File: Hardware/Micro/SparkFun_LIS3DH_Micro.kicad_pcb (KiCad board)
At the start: 2 copper layers, 19 x 7.6 mm, 34 parts, among them J1 PTH_1x1mm, J2 Qwiic_RA, J5 PTH_1x1mm, U1 LIS3DH

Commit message: Fixes silk on micro, and adds note about 22AWG wire with PTH
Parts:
- removed kibuzzard-6841DB16: G***, kibuzzard-6841DB16
- removed kibuzzard-6841DB2D: G***, kibuzzard-6841DB2D
- added kibuzzard-68489829: G***, kibuzzard-68489829, F.Cu at (126.1, 109.5)
- added kibuzzard-68489831: G***, kibuzzard-68489831, F.Cu at (126.2, 104.6)

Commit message: Updates LIS3DH in the micro board according to new changes
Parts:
- U1: footprint SparkFun-Sensor:LGA-16-3X3 -> SparkFun-Sensor:ST_LGA-16_3x3mm_P0.5mm_5x3
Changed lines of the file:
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@@
 		(property ki_fp_filters "Fiducial*")
 		(sheetname "/")
-		(sheetfile "SparkFun_LIS3DH_Mini.kicad_sch")
+		(sheetfile "SparkFun_LIS3DH_Micro.kicad_sch")
 		(attr smd)
 		(fp_circle
@@
 				(font
 					(size 0.001 0.001)
+					(thickness 0.15)
 				)
 			)
@@
 				(font
 					(size 0.001 0.001)
+					(thickness 0.15)
 				)
 			)
@@
 		(property ki_fp_filters "R_*")
 		(sheetname "/")
-		(sheetfile "SparkFun_LIS3DH_Mini.kicad_sch")
+		(sheetfile "SparkFun_LIS3DH_Micro.kicad_sch")
 		(attr smd)
 		(fp_line
@@
 		(property ki_fp_filters "Connector*:*_1x??_*")
 		(sheetname "/")
-		(sheetfile "SparkFun_LIS3DH_Mini.kicad_sch")
+		(sheetfile "SparkFun_LIS3DH_Micro.kicad_sch")
 		(fp_poly
 			(pts
@@
 		(property ki_fp_filters "Connector*:*_1x??_*")
 		(sheetname "/")
-		(sheetfile "SparkFun_LIS3DH_Mini.kicad_sch")
+		(sheetfile "SparkFun_LIS3DH_Micro.kicad_sch")
 		(fp_poly
 			(pts
@@
 		(property ki_fp_filters "R_*")
 		(sheetname "/")
-		(sheetfile "SparkFun_LIS3DH_Mini.kicad_sch")
+		(sheetfile "SparkFun_LIS3DH_Micro.kicad_sch")
 		(attr smd)
 		(fp_line
@@
 		(property ki_fp_filters "R_*")
 		(sheetname "/")
-		(sheetfile "SparkFun_LIS3DH_Mini.kicad_sch")
+		(sheetfile "SparkFun_LIS3DH_Micro.kicad_sch")
 		(attr smd)
 		(fp_line
@@
 		(property ki_fp_filters "LED* LED_SMD:* LED_THT:*")
 		(sheetname "/")
-		(sheetfile "SparkFun_LIS3DH_Mini.kicad_sch")
+		(sheetfile "SparkFun_LIS3DH_Micro.kicad_sch")
 		(attr smd)
 		(fp_line
@@
 		(property ki_fp_filters "Fiducial*")
 		(sheetname "/")
-		(sheetfile "SparkFun_LIS3DH_Mini.kicad_sch")
+		(sheetfile "SparkFun_LIS3DH_Micro.kicad_sch")
 		(attr smd)
 		(fp_circle
@@
 		(property ki_fp_filters "C_*")
 		(sheetname "/")
-		(sheetfile "SparkFun_LIS3DH_Mini.kicad_sch")
+		(sheetfile "SparkFun_LIS3DH_Micro.kicad_sch")
 		(attr smd)
 		(fp_line
@@
 		)
 	)
-	(footprint "SparkFun-Sensor:LGA-16-3X3"
+	(footprint "SparkFun-Sensor:ST_LGA-16_3x3mm_P0.5mm_5x3"
 		(layer "F.Cu")
 		(at 132.156 106.996 180)
-		(descr "16-Pin Land Grid Array (LGA) (3 x 3 mm)\n\nhttps://www.sparkfun.com/datasheets/Sensors/Accelerometer/LIS331HH.pdf Datasheet\n\nSpecifications:\n\n• Pin Count: 16\n• Area: 3.0 x 3.0 x 1.0 mm\n• Pitch: 0.5 mm\n\nDevices Using:\n\n• LIS331\n• LIS3DH")
+		(descr "ST 16-Pin Land Grid Array (LGA) (3 x 3 mm)")
+		(tags "SparkFun")
 		(property "Reference" "U1"
 			(at 0 -1.905 180)
 			(unlocked yes)
 			(layer "F.Fab")
-			(hide yes)
 			(effects
 				(font
@@
 			(unlocked yes)
 			(layer "F.Fab")
-			(hide yes)
 			(effects
 				(font
@@
 		)
 		(property "Datasheet" "https://www.st.com/en/mems-and-sensors/lis3dh.html"
-			(at 0 0 0)
+			(at 0 0 180)
 			(layer "F.Fab")
 			(hide yes)
@@
 		)
 		(property "Description" "The LIS3DH has dynamically user-selectable full scales of ±2g/±4g/±8g/±16g and is capable of measuring accelerations with output data rates from 1 Hz to 5.3 kHz."
-			(at 0 0 0)
+			(at 0 0 180)
 			(layer "F.Fab")
 			(hide yes)
@@
 		)
 		(sheetname "/")
-		(sheetfile "SparkFun_LIS3DH_Mini.kicad_sch")
+		(sheetfile "SparkFun_LIS3DH_Micro.kicad_sch")
 		(fp_line
 			(start 1.7 1.3722)
@@
 		)
 		(fp_circle
-			(center -2.2 -1.6)
-			(end -2.073 -1.6)
+			(center -2.2 -1.5)
+			(end -2.3 -1.5)
 			(stroke
-				(width 0.254)
+				(width 0.2)
 				(type solid)
 			)
@@
 		)
 		(fp_line
+			(start 0 1)
+			(end 0.2 0.8)
+			(stroke
+				(width 0.1)
+				(type default)
+			)
+			(layer "F.Fab")
+		)
+		(fp_line
+			(start 0 1)
+			(end -0.2 0.8)
+			(stroke
+				(width 0.1)
+				(type default)
+			)
+			(layer "F.Fab")
+		)
+		(fp_line
+			(start 0 0)
+			(end 0 1)
+			(stroke
+				(width 0.1)
+				(type default)
+			)
+			(layer "F.Fab")
+		)
+		(fp_line
+			(start 0 0)
+			(end -1 0)
+			(stroke
+				(width 0.1)
+				(type default)
+			)
+			(layer "F.Fab")
+		)
+		(fp_line
+			(start -1 0)
+			(end -0.8 0.2)
+			(stroke
+				(width 0.1)
+				(type default)
+			)
+			(layer "F.Fab")
+		)
+		(fp_line
+			(start -1 0)
+			(end -0.8 -0.2)
+			(stroke
+				(width 0.1)
+				(type default)
+			)
+			(layer "F.Fab")
+		)
+		(fp_line
 			(start -1.5 1.5)
 			(end -1.5 -1.5)
@@
 			(layer "F.Fab")
 		)
+		(fp_circle
+			(center 0 0)
+			(end -0.05 0)
+			(stroke
+				(width 0.1)
+				(type default)
+			)
+			(fill no)
+			(layer "F.Fab")
+		)
+		(fp_circle
+			(center 0 0)
+			(end -0.25 0)
+			(stroke
+				(width 0.1)
+				(type default)
+			)
+			(fill no)
+			(layer "F.Fab")
+		)
+		(fp_text user "Z"
+			(at 0.4 -0.35 180)
+			(unlocked yes)
+			(layer "F.Fab")
+			(effects
+				(font
+					(size 0.25 0.25)
+					(thickness 0.0625)
+				)
+			)
+		)
+		(fp_text user "X"
+			(at -0.8 -0.5 180)
+			(unlocked yes)
+			(layer "F.Fab")
+			(effects
+				(font
+					(size 0.25 0.25)
+					(thickness 0.0625)
+				)
+			)
+		)
+		(fp_text user "Y"
+			(at 0.25 0.5 180)
+			(unlocked yes)
+			(layer "F.Fab")
+			(effects
+				(font
+					(size 0.25 0.25)
+					(thickness 0.0625)
+				)
+			)
+		)
 		(pad "1" smd rect
 			(at -1.4 -1)
@@
 		)
 		(embedded_fonts no)
-		(model "${SPARKFUN_KICAD_LIBRARY}/Footprints/SparkFun-3D-models/Sensor/LIS3DH_LGA-16_3x3x1mm.step"
+		(model "${SPARKFUN_KICAD_LIBRARY}/Footprints/SparkFun-3D-models/Semiconductor-Standard/LGA-16_3x3x1mm.step"
 			(offset
 				(xyz 0 0 0)
@@
 		(property ki_fp_filters "Connector*:*_1x??_*")
 		(sheetname "/")
-		(sheetfile "SparkFun_LIS3DH_Mini.kicad_sch")
+		(sheetfile "SparkFun_LIS3DH_Micro.kicad_sch")
 		(attr smd)
 		(fp_line
@@
 		(property ki_fp_filters "R_*")
 		(sheetname "/")
-		(sheetfile "SparkFun_LIS3DH_Mini.kicad_sch")
+		(sheetfile "SparkFun_LIS3DH_Micro.kicad_sch")
 		(attr smd)
 		(fp_line
@@
 				(font
 					(size 0.001 0.001)
+					(thickness 0.15)
 				)
 			)
@@
 				(font
 					(size 0.001 0.001)
+					(thickness 0.15)
 				)
 			)
@@
 		)
 		(sheetname "/")
-		(sheetfile "SparkFun_LIS3DH_Mini.kicad_sch")
+		(sheetfile "SparkFun_LIS3DH_Micro.kicad_sch")
 		(attr exclude_from_pos_files exclude_from_bom)
 		(fp_text user " https://creativecommons.org/licenses/by-sa/4.0/"
@@
 		(property ki_fp_filters "C_*")
 		(sheetname "/")
-		(sheetfile "SparkFun_LIS3DH_Mini.kicad_sch")
+		(sheetfile "SparkFun_LIS3DH_Micro.kicad_sch")
 		(attr smd)
 		(fp_line
@@
 		(property ki_fp_filters "Fiducial*")
 		(sheetname "/")
-		(sheetfile "SparkFun_LIS3DH_Mini.kicad_sch")
+		(sheetfile "SparkFun_LIS3DH_Micro.kicad_sch")
 		(fp_circle
 			(center 0 0)
@@
 		(property ki_fp_filters "SolderJumper*Open*")
 		(sheetname "/")
-		(sheetfile "SparkFun_LIS3DH_Mini.kicad_sch")
+		(sheetfile "SparkFun_LIS3DH_Micro.kicad_sch")
 		(fp_line
 			(start 1.1176 -0.762)
@@
 		(property ki_fp_filters "SolderJumper*Bridged123*")
 		(sheetname "/")
-		(sheetfile "SparkFun_LIS3DH_Mini.kicad_sch")
+		(sheetfile "SparkFun_LIS3DH_Micro.kicad_sch")
 		(attr allow_soldermask_bridges)
 		(net_tie_pad_groups "1,2,3")
@@
 		(property ki_fp_filters "Pin* Test*")
 		(sheetname "/")
-		(sheetfile "SparkFun_LIS3DH_Mini.kicad_sch")
+		(sheetfile "SparkFun_LIS3DH_Micro.kicad_sch")
 		(fp_circle
 			(center 0 0)
@@
 		(property ki_fp_filters "Pin* Test*")
 		(sheetname "/")
-		(sheetfile "SparkFun_LIS3DH_Mini.kicad_sch")
+		(sheetfile "SparkFun_LIS3DH_Micro.kicad_sch")
 		(fp_circle
 			(center 0 0)
@@
 		(property ki_fp_filters "SolderJumper*Bridged*")
 		(sheetname "/")
-		(sheetfile "SparkFun_LIS3DH_Mini.kicad_sch")
+		(sheetfile "SparkFun_LIS3DH_Micro.kicad_sch")
 		(attr allow_soldermask_bridges)
 		(net_tie_pad_groups "1,2")
@@
 		(property ki_fp_filters "Fiducial*")
 		(sheetname "/")
-		(sheetfile "SparkFun_LIS3DH_Mini.kicad_sch")
+		(sheetfile "SparkFun_LIS3DH_Micro.kicad_sch")
 		(attr smd)
 		(fp_circle
@@
 		(property ki_fp_filters "Fiducial*")
 		(sheetname "/")
-		(sheetfile "SparkFun_LIS3DH_Mini.kicad_sch")
+		(sheetfile "SparkFun_LIS3DH_Micro.kicad_sch")
 		(attr smd)
 		(fp_circle
@@
 		(property ki_fp_filters "Pin* Test*")
 		(sheetname "/")
-		(sheetfile "SparkFun_LIS3DH_Mini.kicad_sch")
+		(sheetfile "SparkFun_LIS3DH_Micro.kicad_sch")
 		(fp_circle
 			(center 0 0)
@@
 		(property ki_fp_filters "Pin* Test*")
 		(sheetname "/")
-		(sheetfile "SparkFun_LIS3DH_Mini.kicad_sch")
+		(sheetfile "SparkFun_LIS3DH_Micro.kicad_sch")
 		(fp_circle
 			(center 0 0)

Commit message: Updates the 1 mm PTH part
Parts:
- D1: footprint SparkFun-LED:LED_0402_1005Metric -> SparkFun-LED:LED_0402_1005Metric_Red
- J1, J5: footprint SparkFun-Connector:1x01_PTH_1x1mm -> SparkFun-Connector:1x01_1x1mm
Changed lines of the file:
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@@
 		)
 	)
-	(footprint "SparkFun-Connector:1x01_PTH_1x1mm"
+	(footprint "SparkFun-Connector:1x01_1x1mm"
 		(layer "F.Cu")
 		(at 128.346 104.456 180)
 		(descr "Plated Through Hole - No Silk Outline\n\nSpecifications:\n\n• Pin count:1\n• Pin pitch:0.1mm\n• Hole Size: .7mm\n• Annular Ring: 1.2mm\n\nMade for the small  https://www.sparkfun.com/products/18221  1mm Pitch Headers.")
+		(tags "SparkFun")
 		(property "Reference" "J5"
 			(at 0 -0.889 180)
@@
 		)
 		(property "Datasheet" ""
-			(at 0 0 0)
+			(at 0 0 180)
 			(layer "F.Fab")
 			(hide yes)
@@
 		)
 		(property "Description" ""
-			(at 0 0 0)
+			(at 0 0 180)
 			(layer "F.Fab")
 			(hide yes)
@@
 		(sheetname "/")
 		(sheetfile "SparkFun_LIS3DH_Micro.kicad_sch")
+		(fp_rect
+			(start -1 -1)
+			(end 1 1)
+			(stroke
+				(width 0.05)
+				(type default)
+			)
+			(fill no)
+			(layer "F.CrtYd")
+		)
 		(fp_poly
 			(pts
@@
 		(embedded_fonts no)
 	)
-	(footprint "SparkFun-Connector:1x01_PTH_1x1mm"
+	(footprint "SparkFun-Connector:1x01_1x1mm"
 		(layer "F.Cu")
 		(at 128.346 109.536 180)
 		(descr "Plated Through Hole - No Silk Outline\n\nSpecifications:\n\n• Pin count:1\n• Pin pitch:0.1mm\n• Hole Size: .7mm\n• Annular Ring: 1.2mm\n\nMade for the small  https://www.sparkfun.com/products/18221  1mm Pitch Headers.")
+		(tags "SparkFun")
 		(property "Reference" "J1"
 			(at 0 -0.889 180)
@@
 		)
 		(property "Datasheet" ""
-			(at 0 0 0)
+			(at 0 0 180)
 			(layer "F.Fab")
 			(hide yes)
@@
 		)
 		(property "Description" ""
-			(at 0 0 0)
+			(at 0 0 180)
 			(layer "F.Fab")
 			(hide yes)
@@
 		(sheetname "/")
 		(sheetfile "SparkFun_LIS3DH_Micro.kicad_sch")
+		(fp_rect
+			(start -1 -1)
+			(end 1 1)
+			(stroke
+				(width 0.05)
+				(type default)
+			)
+			(fill no)
+			(layer "F.CrtYd")
+		)
 		(fp_poly
 			(pts
@@
 		)
 	)
-	(footprint "SparkFun-LED:LED_0402_1005Metric"
+	(footprint "SparkFun-LED:LED_0402_1005Metric_Red"
 		(layer "F.Cu")
 		(at 131.2035 104.1385)
@@
 			)
 		)
-		(property "PROD_ID" "DIO-25000"
+		(property "PROD_ID" "DIO-16757"
 			(at 0 0 0)
 			(unlocked yes)
@@
 		)
 		(embedded_fonts no)
-		(model "${KICAD6_3DMODEL_DIR}/LED_SMD.3dshapes/LED_0402_1005Metric.wrl"
+		(model "${SPARKFUN_KICAD_LIBRARY}/Footprints/SparkFun-3D-models/LED/LED_0402_1005Metric_Red.step"
 			(offset
 				(xyz 0 0 0)

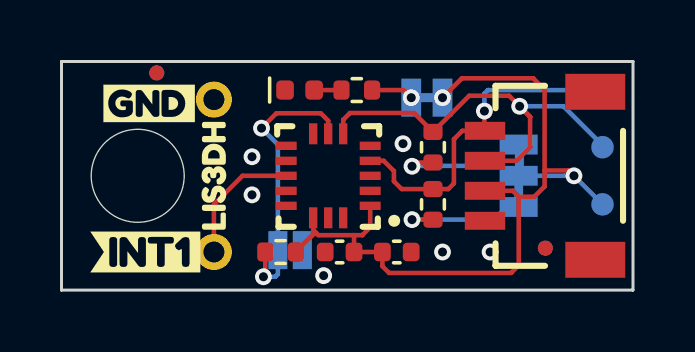
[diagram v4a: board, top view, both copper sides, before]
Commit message: Adds axes to design
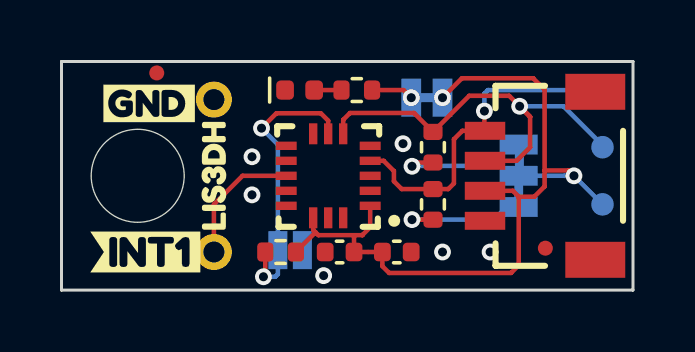
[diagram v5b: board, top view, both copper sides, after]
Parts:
- removed FID1, FID2: Fiducial_0.5mm, SparkFun-Aesthetic:Fiducial_0.5mm_Mask1mm
- removed the G*** at (133.3, 107.0)
- added G***: Flame, SparkFun-Aesthetic:SparkFun_Flame_2.5mm, B.Cu at (124.2, 104.5)
- added kibuzzard-685C51A0: G***, kibuzzard-685C51A0, B.Cu at (135.6, 107.1)
- added kibuzzard-685C52CC: G***, kibuzzard-685C52CC, B.Cu at (132.1, 105.6)
- added kibuzzard-685C52E1: G***, kibuzzard-685C52E1, B.Cu at (132.9, 108.7)

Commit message: Removes gyroscopic arrows from silk - this is an accelerometer 😝
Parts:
- moved kibuzzard-685C52E1 0.64 mm to (133.0, 108.1)
- moved kibuzzard-685C52CC 0.06 mm to (132.0, 105.6)
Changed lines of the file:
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@@
 			(psa4output no)
 			(plot_black_and_white yes)
+			(plotinvisibletext no)
 			(sketchpadsonfab no)
 			(plotpadnumbers no)
@@
 	(footprint "kibuzzard-685C52CC"
 		(layer "B.Cu")
-		(at 132.093033 105.572004 180)
+		(at 132.029 105.572004 180)
 		(descr "Generated with KiBuzzard")
 		(tags "kb_params=eyJBbGlnbm1lbnRDaG9pY2UiOiAiQ2VudGVyIiwgIkNhcExlZnRDaG9pY2UiOiAiKCIsICJDYXBSaWdodENob2ljZSI6ICJdIiwgIkZvbnRDb21ib0JveCI6ICJGcmVkZHlTcGFyay1SZWd1bGFyIiwgIkhlaWdodEN0cmwiOiAwLjksICJMYXllckNvbWJvQm94IjogIkYuU2lsa1MiLCAiTGluZVNwYWNpbmdDdHJsIjogMS41LCAiTXVsdGlMaW5lVGV4dCI6ICJZIiwgIlBhZGRpbmdCb3R0b21DdHJsIjogMS41LCAiUGFkZGluZ0xlZnRDdHJsIjogNi4wLCAiUGFkZGluZ1JpZ2h0Q3RybCI6IDEuNSwgIlBhZGRpbmdUb3BDdHJsIjogMS41LCAiV2lkdGhDdHJsIjogMS4wLCAiYWR2YW5jZWRDaGVja2JveCI6IHRydWUsICJpbmxpbmVGb3JtYXRUZXh0Ym94IjogdHJ1ZSwgImxpbmVvdmVyU3R5bGVDaG9pY2UiOiAiU3F1YXJlIiwgImxpbmVvdmVyVGhpY2tuZXNzQ3RybCI6IDF9")
@@
 			(fill yes)
 			(layer "B.SilkS")
-			(net 78)
 		)
 		(embedded_fonts no)
@@
 	(footprint "kibuzzard-685C52E1"
 		(layer "B.Cu")
-		(at 132.858462 108.747004 180)
+		(at 133.045 108.139 180)
 		(descr "Generated with KiBuzzard")
 		(tags "kb_params=eyJBbGlnbm1lbnRDaG9pY2UiOiAiQ2VudGVyIiwgIkNhcExlZnRDaG9pY2UiOiAiKCIsICJDYXBSaWdodENob2ljZSI6ICJdIiwgIkZvbnRDb21ib0JveCI6ICJGcmVkZHlTcGFyay1SZWd1bGFyIiwgIkhlaWdodEN0cmwiOiAwLjksICJMYXllckNvbWJvQm94IjogIkYuU2lsa1MiLCAiTGluZVNwYWNpbmdDdHJsIjogMS41LCAiTXVsdGlMaW5lVGV4dCI6ICJaIiwgIlBhZGRpbmdCb3R0b21DdHJsIjogMS41LCAiUGFkZGluZ0xlZnRDdHJsIjogNi4wLCAiUGFkZGluZ1JpZ2h0Q3RybCI6IDEuNSwgIlBhZGRpbmdUb3BDdHJsIjogMS41LCAiV2lkdGhDdHJsIjogMS4wLCAiYWR2YW5jZWRDaGVja2JveCI6IHRydWUsICJpbmxpbmVGb3JtYXRUZXh0Ym94IjogdHJ1ZSwgImxpbmVvdmVyU3R5bGVDaG9pY2UiOiAiU3F1YXJlIiwgImxpbmVvdmVyVGhpY2tuZXNzQ3RybCI6IDF9")
@@
 			(fill yes)
 			(layer "B.SilkS")
-			(net 78)
 		)
 		(embedded_fonts no)
@@
 			(fill yes)
 			(layer "B.SilkS")
-			(net 78)
 		)
 		(embedded_fonts no)
@@
 		(layer "B.SilkS")
 	)
-	(gr_arc
-		(start 133.998033 106.534225)
-		(mid 134.3785 106.996)
-		(end 134.196003 107.565812)
-		(stroke
-			(width 0.15)
-			(type default)
-		)
-		(layer "B.SilkS")
-	)
-	(gr_line
-		(start 133.959214 106.558931)
-		(end 133.998033 106.839025)
-		(stroke
-			(width 0.15)
-			(type default)
-		)
-		(layer "B.SilkS")
-	)
-	(gr_line
-		(start 132.572238 106.372383)
-		(end 132.372433 106.178625)
-		(stroke
-			(width 0.15)
-			(type default)
-		)
-		(layer "B.SilkS")
-	)
-	(gr_line
-		(start 132.858459 107.854239)
-		(end 132.651833 107.546013)
-		(stroke
-			(width 0.15)
-			(type default)
-		)
-		(layer "B.SilkS")
-	)
-	(gr_line
-		(start 132.572238 106.372383)
-		(end 132.829633 106.280225)
-		(stroke
-			(width 0.15)
-			(type default)
-		)
-		(layer "B.SilkS")
-	)
-	(gr_arc
-		(start 132.572238 106.372383)
-		(mid 133.06277 105.920551)
-		(end 133.490033 106.432625)
-		(stroke
-			(width 0.15)
-			(type default)
-		)
-		(layer "B.SilkS")
-	)
 	(gr_line
 		(start 133.009408 106.680438)
@@
 		(layer "B.SilkS")
 	)
-	(gr_line
-		(start 133.993414 106.524431)
-		(end 134.307453 106.442419)
-		(stroke
-			(width 0.15)
-			(type default)
-		)
-		(layer "B.SilkS")
-	)
 	(gr_poly
 		(pts
@@
 		(layer "B.SilkS")
 	)
-	(gr_line
-		(start 132.858459 107.876739)
-		(end 132.550233 108.025713)
-		(stroke
-			(width 0.15)
-			(type default)
-		)
-		(layer "B.SilkS")
-	)
 	(gr_poly
 		(pts
@@
 		(layer "B.SilkS")
 	)
-	(gr_arc
-		(start 132.858459 107.854239)
-		(mid 132.193372 107.360282)
-		(end 132.474033 106.580813)
-		(stroke
-			(width 0.15)
-			(type default)
-		)
-		(layer "B.SilkS")
-	)
